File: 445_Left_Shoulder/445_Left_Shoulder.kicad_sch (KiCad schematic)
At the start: 2 parts, among them J1 69167-107HLF, U1 LSM6DSMTR

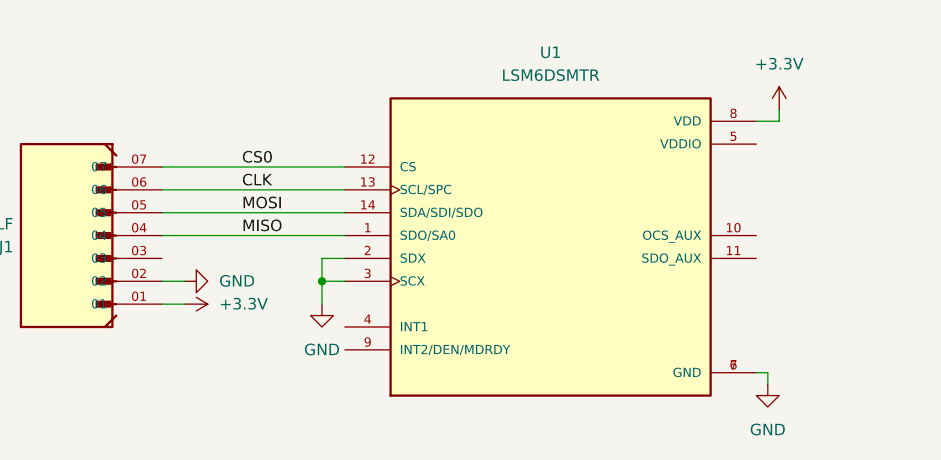
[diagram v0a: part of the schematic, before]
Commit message: Added filtering caps and int line
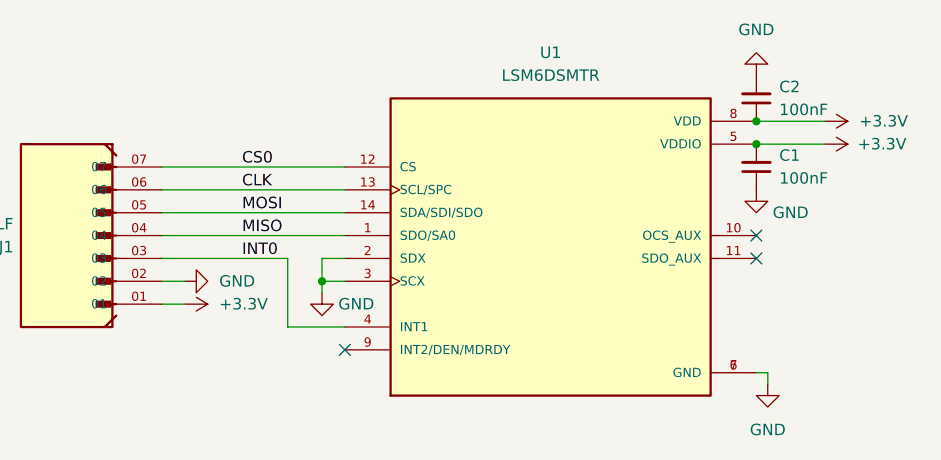
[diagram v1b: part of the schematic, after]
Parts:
- added C1, C2: 100nF, symbol Device:C_Small
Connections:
- net +3.3V: now also U1.5 (VDDIO), C1.2, C2.1
- net GND: now also C1.1, C2.2
- net INT0: now reaches J1.03
- net INT0: now also U1.4 (INT1)
- no-connect marks 0 -> 3
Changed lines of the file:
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@@
 (kicad_sch (version 20230121) (generator eeschema)
   (paper "A4")
+  (junction (at 186.69 74.93) (diameter 0) (color 0 0 0 0)
+  )
+  (junction (at 186.69 72.39) (diameter 0) (color 0 0 0 0)
+  )
   (junction (at 138.43 90.17) (diameter 0) (color 0 0 0 0)
   )
-  (wire (pts (xy 138.43 90.17) (xy 138.43 92.71))
+  (no_connect (at 140.97 97.79))
+  (no_connect (at 186.69 85.09))
+  (no_connect (at 186.69 87.63))
+  (wire (pts (xy 138.43 90.17) (xy 138.43 91.44))
+    (stroke (width 0) (type default))
+  )
+  (wire (pts (xy 186.69 74.93) (xy 194.31 74.93))
     (stroke (width 0) (type default))
   )
@@
     (stroke (width 0) (type default))
   )
+  (wire (pts (xy 134.62 87.63) (xy 120.65 87.63))
+    (stroke (width 0) (type default))
+  )
   (wire (pts (xy 138.43 87.63) (xy 138.43 90.17))
     (stroke (width 0) (type default))
@@
     (stroke (width 0) (type default))
   )
+  (wire (pts (xy 140.97 95.25) (xy 134.62 95.25))
+    (stroke (width 0) (type default))
+  )
   (wire (pts (xy 120.65 80.01) (xy 140.97 80.01))
     (stroke (width 0) (type default))
@@
     (stroke (width 0) (type default))
   )
-  (wire (pts (xy 189.23 72.39) (xy 189.23 71.12))
-    (stroke (width 0) (type default))
-  )
-  (wire (pts (xy 186.69 72.39) (xy 189.23 72.39))
+  (wire (pts (xy 134.62 95.25) (xy 134.62 87.63))
     (stroke (width 0) (type default))
   )
@@
   )
   (wire (pts (xy 120.65 82.55) (xy 140.97 82.55))
+    (stroke (width 0) (type default))
+  )
+  (wire (pts (xy 186.69 72.39) (xy 194.31 72.39))
     (stroke (width 0) (type default))
   )
@@
     (effects (font (size 1.27 1.27)) (justify left bottom))
   )
-  (symbol (lib_id "power:+3.3V") (at 189.23 71.12 0) (unit 1)
-    (in_bom yes) (on_board yes) (dnp no) (fields_autoplaced)
-    (property "Reference" "#PWR05" (at 189.23 74.93 0)
-      (effects (font (size 1.27 1.27)) hide)
-    )
-    (property "Value" "+3.3V" (at 189.23 66.04 0)
-      (effects (font (size 1.27 1.27)))
-    )
-    (property "Footprint" "" (at 189.23 71.12 0)
-      (effects (font (size 1.27 1.27)) hide)
-    )
-    (property "Datasheet" "" (at 189.23 71.12 0)
+  (label "INT0" (at 129.54 87.63 0) (fields_autoplaced)
+    (effects (font (size 1.27 1.27)) (justify left bottom))
+  )
+  (symbol (lib_id "power:+3.3V") (at 194.31 72.39 270) (unit 1)
+    (in_bom yes) (on_board yes) (dnp no) (fields_autoplaced)
+    (property "Reference" "#PWR05" (at 190.5 72.39 0)
+      (effects (font (size 1.27 1.27)) hide)
+    )
+    (property "Value" "+3.3V" (at 198.12 72.39 90)
+      (effects (font (size 1.27 1.27)) (justify left))
+    )
+    (property "Footprint" "" (at 194.31 72.39 0)
+      (effects (font (size 1.27 1.27)) hide)
+    )
+    (property "Datasheet" "" (at 194.31 72.39 0)
       (effects (font (size 1.27 1.27)) hide)
     )
@@
     )
   )
-  (symbol (lib_id "power:GND") (at 138.43 92.71 0) (unit 1)
-    (in_bom yes) (on_board yes) (dnp no) (fields_autoplaced)
-    (property "Reference" "#PWR03" (at 138.43 99.06 0)
-      (effects (font (size 1.27 1.27)) hide)
-    )
-    (property "Value" "GND" (at 138.43 97.79 0)
-      (effects (font (size 1.27 1.27)))
-    )
-    (property "Footprint" "" (at 138.43 92.71 0)
-      (effects (font (size 1.27 1.27)) hide)
-    )
-    (property "Datasheet" "" (at 138.43 92.71 0)
+  (symbol (lib_id "power:GND") (at 138.43 91.44 0) (unit 1)
+    (in_bom yes) (on_board yes) (dnp no)
+    (property "Reference" "#PWR03" (at 138.43 97.79 0)
+      (effects (font (size 1.27 1.27)) hide)
+    )
+    (property "Value" "GND" (at 142.24 92.71 0)
+      (effects (font (size 1.27 1.27)))
+    )
+    (property "Footprint" "" (at 138.43 91.44 0)
+      (effects (font (size 1.27 1.27)) hide)
+    )
+    (property "Datasheet" "" (at 138.43 91.44 0)
       (effects (font (size 1.27 1.27)) hide)
     )
@@
         (path "/f3411692-45b2-468b-a86a-802fc626f60f"
           (reference "#PWR03") (unit 1)
+        )
+      )
+    )
+  )
+  (symbol (lib_id "Device:C_Small") (at 186.69 69.85 180) (unit 1)
+    (in_bom yes) (on_board yes) (dnp no) (fields_autoplaced)
+    (property "Reference" "C2" (at 189.23 68.5736 0)
+      (effects (font (size 1.27 1.27)) (justify right))
+    )
+    (property "Value" "100nF" (at 189.23 71.1136 0)
+      (effects (font (size 1.27 1.27)) (justify right))
+    )
+    (property "Footprint" "" (at 186.69 69.85 0)
+      (effects (font (size 1.27 1.27)) hide)
+    )
+    (property "Datasheet" "~" (at 186.69 69.85 0)
+      (effects (font (size 1.27 1.27)) hide)
+    )
+    (pin "1")
+    (pin "2")
+    (instances
+      (project "445_Left_Shoulder"
+        (path "/f3411692-45b2-468b-a86a-802fc626f60f"
+          (reference "C2") (unit 1)
+        )
+      )
+    )
+  )
+  (symbol (lib_id "power:+3.3V") (at 194.31 74.93 270) (unit 1)
+    (in_bom yes) (on_board yes) (dnp no)
+    (property "Reference" "#PWR06" (at 190.5 74.93 0)
+      (effects (font (size 1.27 1.27)) hide)
+    )
+    (property "Value" "+3.3V" (at 200.66 74.93 90)
+      (effects (font (size 1.27 1.27)))
+    )
+    (property "Footprint" "" (at 194.31 74.93 0)
+      (effects (font (size 1.27 1.27)) hide)
+    )
+    (property "Datasheet" "" (at 194.31 74.93 0)
+      (effects (font (size 1.27 1.27)) hide)
+    )
+    (pin "1")
+    (instances
+      (project "445_Left_Shoulder"
+        (path "/f3411692-45b2-468b-a86a-802fc626f60f"
+          (reference "#PWR06") (unit 1)
         )
       )
@@
         (path "/f3411692-45b2-468b-a86a-802fc626f60f"
           (reference "#PWR04") (unit 1)
+        )
+      )
+    )
+  )
+  (symbol (lib_id "Device:C_Small") (at 186.69 77.47 180) (unit 1)
+    (in_bom yes) (on_board yes) (dnp no) (fields_autoplaced)
+    (property "Reference" "C1" (at 189.23 76.1936 0)
+      (effects (font (size 1.27 1.27)) (justify right))
+    )
+    (property "Value" "100nF" (at 189.23 78.7336 0)
+      (effects (font (size 1.27 1.27)) (justify right))
+    )
+    (property "Footprint" "" (at 186.69 77.47 0)
+      (effects (font (size 1.27 1.27)) hide)
+    )
+    (property "Datasheet" "~" (at 186.69 77.47 0)
+      (effects (font (size 1.27 1.27)) hide)
+    )
+    (pin "1")
+    (pin "2")
+    (instances
+      (project "445_Left_Shoulder"
+        (path "/f3411692-45b2-468b-a86a-802fc626f60f"
+          (reference "C1") (unit 1)
         )
       )
@@
     (pin "01")
     (pin "02")
-    (pin "05")
-    (pin "07")
     (pin "03")
     (pin "04")
+    (pin "05")
     (pin "06")
+    (pin "07")
     (instances
       (project "445_Left_Shoulder"
@@
       (effects (font (size 1.27 1.27)) (justify bottom) hide)
     )
+    (pin "1")
+    (pin "10")
+    (pin "11")
     (pin "12")
-    (pin "5")
-    (pin "9")
-    (pin "3")
-    (pin "1")
-    (pin "11")
-    (pin "6")
     (pin "13")
     (pin "14")
+    (pin "2")
+    (pin "3")
+    (pin "4")
+    (pin "5")
+    (pin "6")
     (pin "7")
     (pin "8")
-    (pin "10")
-    (pin "4")
-    (pin "2")
+    (pin "9")
     (instances
       (project "445_Left_Shoulder"
@@
         )
       )
+    )
+  )
+  (symbol (lib_id "power:GND") (at 186.69 67.31 180) (unit 1)
+    (in_bom yes) (on_board yes) (dnp no) (fields_autoplaced)
+    (property "Reference" "#PWR08" (at 186.69 60.96 0)
+      (effects (font (size 1.27 1.27)) hide)
+    )
+    (property "Value" "GND" (at 186.69 62.23 0)
+      (effects (font (size 1.27 1.27)))
+    )
+    (property "Footprint" "" (at 186.69 67.31 0)
+      (effects (font (size 1.27 1.27)) hide)
+    )
+    (property "Datasheet" "" (at 186.69 67.31 0)
+      (effects (font (size 1.27 1.27)) hide)
+    )
+    (pin "1")
+    (instances
+      (project "445_Left_Shoulder"
+        (path "/f3411692-45b2-468b-a86a-802fc626f60f"
+          (reference "#PWR08") (unit 1)
+        )
+      )
+    )
+  )
+  (symbol (lib_id "power:GND") (at 186.69 80.01 0) (unit 1)
+    (in_bom yes) (on_board yes) (dnp no)
+    (property "Reference" "#PWR07" (at 186.69 86.36 0)
+      (effects (font (size 1.27 1.27)) hide)
+    )
+    (property "Value" "GND" (at 190.5 82.55 0)
+      (effects (font (size 1.27 1.27)))
+    )
+    (property "Footprint" "" (at 186.69 80.01 0)
+      (effects (font (size 1.27 1.27)) hide)
+    )
+    (property "Datasheet" "" (at 186.69 80.01 0)
+      (effects (font (size 1.27 1.27)) hide)
+    )
+    (pin "1")
+    (instances
+      (project "445_Left_Shoulder"
+        (path "/f3411692-45b2-468b-a86a-802fc626f60f"
+          (reference "#PWR07") (unit 1)
+        )
+      )

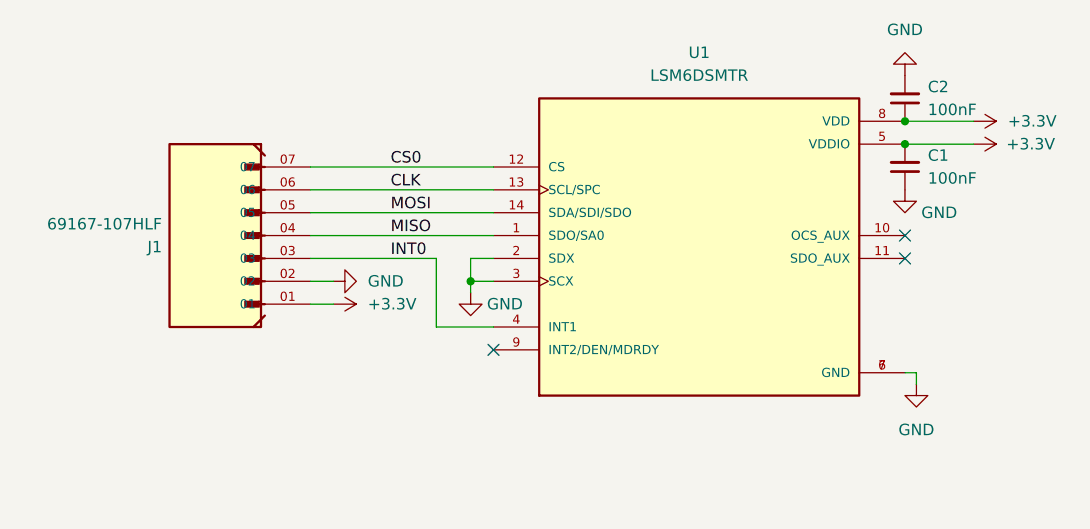
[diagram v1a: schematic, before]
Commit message: enable signal and analog switches
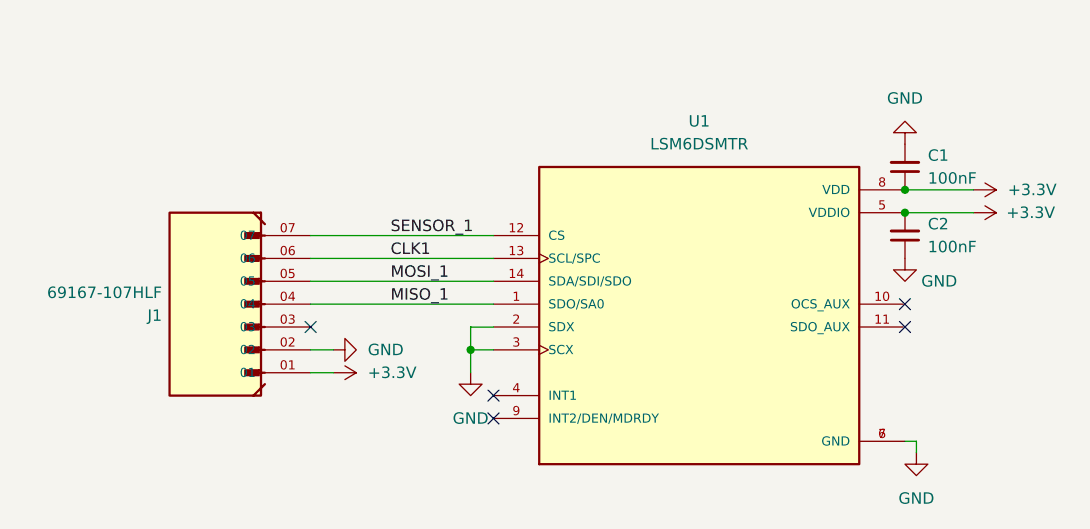
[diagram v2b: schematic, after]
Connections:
- net +3.3V: now also C1.1, C2.2; no longer C1.2, C2.1
- net GND: now also C1.2, C2.1; no longer C1.1, C2.2
- net CLK renamed CLK1
- net CS0 renamed SENSOR_1
- net INT0: no longer names the net of U1.4 (INT1)
- net INT0: no longer J1.03
- net MISO renamed MISO_1
- net MOSI renamed MOSI_1
- no-connect marks 3 -> 5

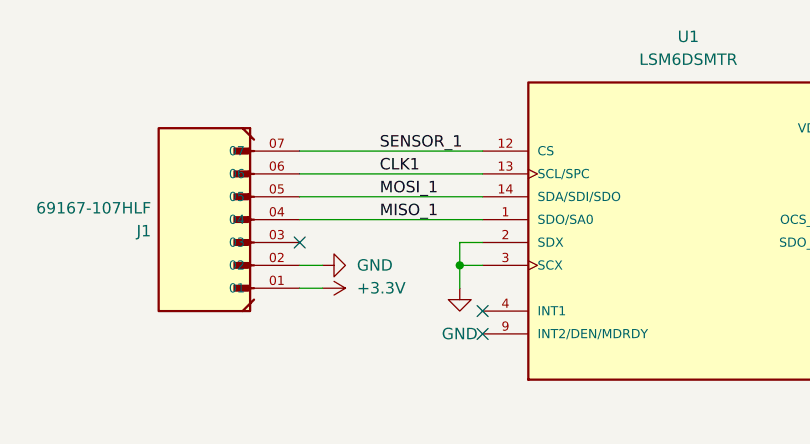
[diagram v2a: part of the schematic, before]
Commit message: replace bicep connector and add int1 connections
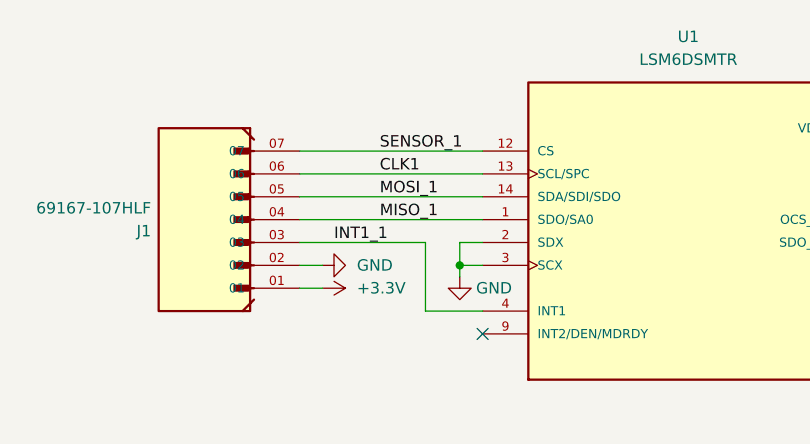
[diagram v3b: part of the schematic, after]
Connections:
- net INT1_1: now reaches U1.4 (INT1)
- net INT1_1: now also J1.03
- no-connect marks 5 -> 3
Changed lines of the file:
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@@
   )
   (no_connect (at 186.69 95.25))
-  (no_connect (at 120.65 95.25))
   (no_connect (at 186.69 92.71))
   (no_connect (at 140.97 105.41))
-  (no_connect (at 140.97 102.87))
+  (wire (pts (xy 134.62 95.25) (xy 134.62 102.87))
+    (stroke (width 0) (type default))
+  )
   (wire (pts (xy 120.65 85.09) (xy 140.97 85.09))
     (stroke (width 0) (type default))
   )
+  (wire (pts (xy 138.43 99.06) (xy 138.43 97.79))
+    (stroke (width 0) (type default))
+  )
   (wire (pts (xy 186.69 107.95) (xy 187.96 107.95))
     (stroke (width 0) (type default))
@@
     (stroke (width 0) (type default))
   )
+  (wire (pts (xy 134.62 102.87) (xy 140.97 102.87))
+    (stroke (width 0) (type default))
+  )
   (wire (pts (xy 186.69 80.01) (xy 194.31 80.01))
     (stroke (width 0) (type default))
@@
     (stroke (width 0) (type default))
   )
-  (wire (pts (xy 138.43 97.79) (xy 138.43 100.33))
+  (wire (pts (xy 120.65 95.25) (xy 134.62 95.25))
     (stroke (width 0) (type default))
   )
@@
   (wire (pts (xy 187.96 107.95) (xy 187.96 109.22))
     (stroke (width 0) (type default))
+  )
+  (label "INT1_1" (at 124.46 95.25 0) (fields_autoplaced)
+    (effects (font (size 1.27 1.27)) (justify left bottom))
   )
   (label "MISO_1" (at 129.54 92.71 0) (fields_autoplaced)
@@
     )
   )
-  (symbol (lib_id "power:GND") (at 138.43 100.33 0) (unit 1)
-    (in_bom yes) (on_board yes) (dnp no) (fields_autoplaced)
-    (property "Reference" "#PWR03" (at 138.43 106.68 0)
-      (effects (font (size 1.27 1.27)) hide)
-    )
-    (property "Value" "GND" (at 138.43 105.41 0)
-      (effects (font (size 1.27 1.27)))
-    )
-    (property "Footprint" "" (at 138.43 100.33 0)
-      (effects (font (size 1.27 1.27)) hide)
-    )
-    (property "Datasheet" "" (at 138.43 100.33 0)
-      (effects (font (size 1.27 1.27)) hide)
-    )
+  (symbol (lib_id "power:GND") (at 138.43 99.06 0) (unit 1)
+    (in_bom yes) (on_board yes) (dnp no)
+    (property "Reference" "#PWR03" (at 138.43 105.41 0)
+      (effects (font (size 1.27 1.27)) hide)
+    )
+    (property "Value" "GND" (at 142.24 100.33 0)
+      (effects (font (size 1.27 1.27)))
+    )
+    (property "Footprint" "" (at 138.43 99.06 0)
+      (effects (font (size 1.27 1.27)) hide)
+    )
+    (property "Datasheet" "" (at 138.43 99.06 0)
+      (effects (font (size 1.27 1.27)) hide)
+    )

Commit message: Layout First Draft
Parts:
- added H1, H2, H3, H4: MountingHole, MountingHole:MountingHole_2mm, symbol Mechanical:MountingHole
- C1, C2: footprint (none) -> CL21F104ZAANNNC:CAPC2012X135N
- renumbered J1 to J2, U1 to U3
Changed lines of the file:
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@@
+    )
+  )
+  (symbol (lib_id "Mechanical:MountingHole") (at 24.13 35.56 0) (unit 1)
+    (in_bom yes) (on_board yes) (dnp no) (fields_autoplaced)
+    (property "Reference" "H2" (at 26.67 34.29 0)
+      (effects (font (size 1.27 1.27)) (justify left))
+    )
+    (property "Value" "MountingHole" (at 26.67 36.83 0)
+      (effects (font (size 1.27 1.27)) (justify left))
+    )
+    (property "Footprint" "MountingHole:MountingHole_2mm" (at 24.13 35.56 0)
+      (effects (font (size 1.27 1.27)) hide)
+    )
+    (property "Datasheet" "~" (at 24.13 35.56 0)
+      (effects (font (size 1.27 1.27)) hide)
+    )
+    (instances
+      (project "445_Left_Shoulder"
+        (path "/f3411692-45b2-468b-a86a-802fc626f60f"
+          (reference "H2") (unit 1)
+        )
+      )
     )
   )
@@
       (effects (font (size 1.27 1.27)) (justify right))
     )
-    (property "Footprint" "" (at 186.69 85.09 0)
+    (property "Footprint" "CL21F104ZAANNNC:CAPC2012X135N" (at 186.69 85.09 0)
       (effects (font (size 1.27 1.27)) hide)
     )
@@
   (symbol (lib_id "LSM6DSMTR:LSM6DSMTR") (at 163.83 92.71 0) (unit 1)
     (in_bom yes) (on_board yes) (dnp no) (fields_autoplaced)
-    (property "Reference" "U1" (at 163.83 72.39 0)
+    (property "Reference" "U3" (at 163.83 72.39 0)
       (effects (font (size 1.27 1.27)))
     )
@@
       (project "445_Left_Shoulder"
         (path "/f3411692-45b2-468b-a86a-802fc626f60f"
-          (reference "U1") (unit 1)
+          (reference "U3") (unit 1)
         )
       )
@@
       (effects (font (size 1.27 1.27)) (justify right))
     )
-    (property "Footprint" "" (at 186.69 77.47 0)
+    (property "Footprint" "CL21F104ZAANNNC:CAPC2012X135N" (at 186.69 77.47 0)
       (effects (font (size 1.27 1.27)) hide)
     )
@@
         (path "/f3411692-45b2-468b-a86a-802fc626f60f"
           (reference "C1") (unit 1)
+        )
+      )
+    )
+  )
+  (symbol (lib_id "Mechanical:MountingHole") (at 24.13 25.4 0) (unit 1)
+    (in_bom yes) (on_board yes) (dnp no) (fields_autoplaced)
+    (property "Reference" "H1" (at 26.67 24.13 0)
+      (effects (font (size 1.27 1.27)) (justify left))
+    )
+    (property "Value" "MountingHole" (at 26.67 26.67 0)
+      (effects (font (size 1.27 1.27)) (justify left))
+    )
+    (property "Footprint" "MountingHole:MountingHole_2mm" (at 24.13 25.4 0)
+      (effects (font (size 1.27 1.27)) hide)
+    )
+    (property "Datasheet" "~" (at 24.13 25.4 0)
+      (effects (font (size 1.27 1.27)) hide)
+    )
+    (instances
+      (project "445_Left_Shoulder"
+        (path "/f3411692-45b2-468b-a86a-802fc626f60f"
+          (reference "H1") (unit 1)
         )
       )
@@
     )
   )
+  (symbol (lib_id "Mechanical:MountingHole") (at 24.13 45.72 0) (unit 1)
+    (in_bom yes) (on_board yes) (dnp no) (fields_autoplaced)
+    (property "Reference" "H3" (at 26.67 44.45 0)
+      (effects (font (size 1.27 1.27)) (justify left))
+    )
+    (property "Value" "MountingHole" (at 26.67 46.99 0)
+      (effects (font (size 1.27 1.27)) (justify left))
+    )
+    (property "Footprint" "MountingHole:MountingHole_2mm" (at 24.13 45.72 0)
+      (effects (font (size 1.27 1.27)) hide)
+    )
+    (property "Datasheet" "~" (at 24.13 45.72 0)
+      (effects (font (size 1.27 1.27)) hide)
+    )
+    (instances
+      (project "445_Left_Shoulder"
+        (path "/f3411692-45b2-468b-a86a-802fc626f60f"
+          (reference "H3") (unit 1)
+        )
+      )
+    )
+  )
+  (symbol (lib_id "Mechanical:MountingHole") (at 24.13 55.88 0) (unit 1)
+    (in_bom yes) (on_board yes) (dnp no) (fields_autoplaced)
+    (property "Reference" "H4" (at 26.67 54.61 0)
+      (effects (font (size 1.27 1.27)) (justify left))
+    )
+    (property "Value" "MountingHole" (at 26.67 57.15 0)
+      (effects (font (size 1.27 1.27)) (justify left))
+    )
+    (property "Footprint" "MountingHole:MountingHole_2mm" (at 24.13 55.88 0)
+      (effects (font (size 1.27 1.27)) hide)
+    )
+    (property "Datasheet" "~" (at 24.13 55.88 0)
+      (effects (font (size 1.27 1.27)) hide)
+    )
+    (instances
+      (project "445_Left_Shoulder"
+        (path "/f3411692-45b2-468b-a86a-802fc626f60f"
+          (reference "H4") (unit 1)
+        )
+      )
+    )
+  )
   (symbol (lib_id "69167-107HLF:69167-107HLF") (at 110.49 92.71 180) (unit 1)
     (in_bom yes) (on_board yes) (dnp no)
-    (property "Reference" "J1" (at 104.14 93.98 0)
+    (property "Reference" "J2" (at 104.14 93.98 0)
       (effects (font (size 1.27 1.27)) (justify left))
     )
@@
       (project "445_Left_Shoulder"
         (path "/f3411692-45b2-468b-a86a-802fc626f60f"
-          (reference "J1") (unit 1)
-        )
-      )
+          (reference "J2") (unit 1)
+        )
+      )
